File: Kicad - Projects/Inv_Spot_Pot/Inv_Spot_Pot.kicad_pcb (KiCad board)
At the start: 2 copper layers, 190 x 179.5 mm, 111 parts, among them J2 PWM, J3 Display_Power, J4 24V, J5 24V, J6 PWM, K1 Y14x-1C-xxDS, Q1 60N60, Q2 60N60, Q3 60N60, Q4 60N60, T1 Transformer_1P_2S, U2 LTV-817S

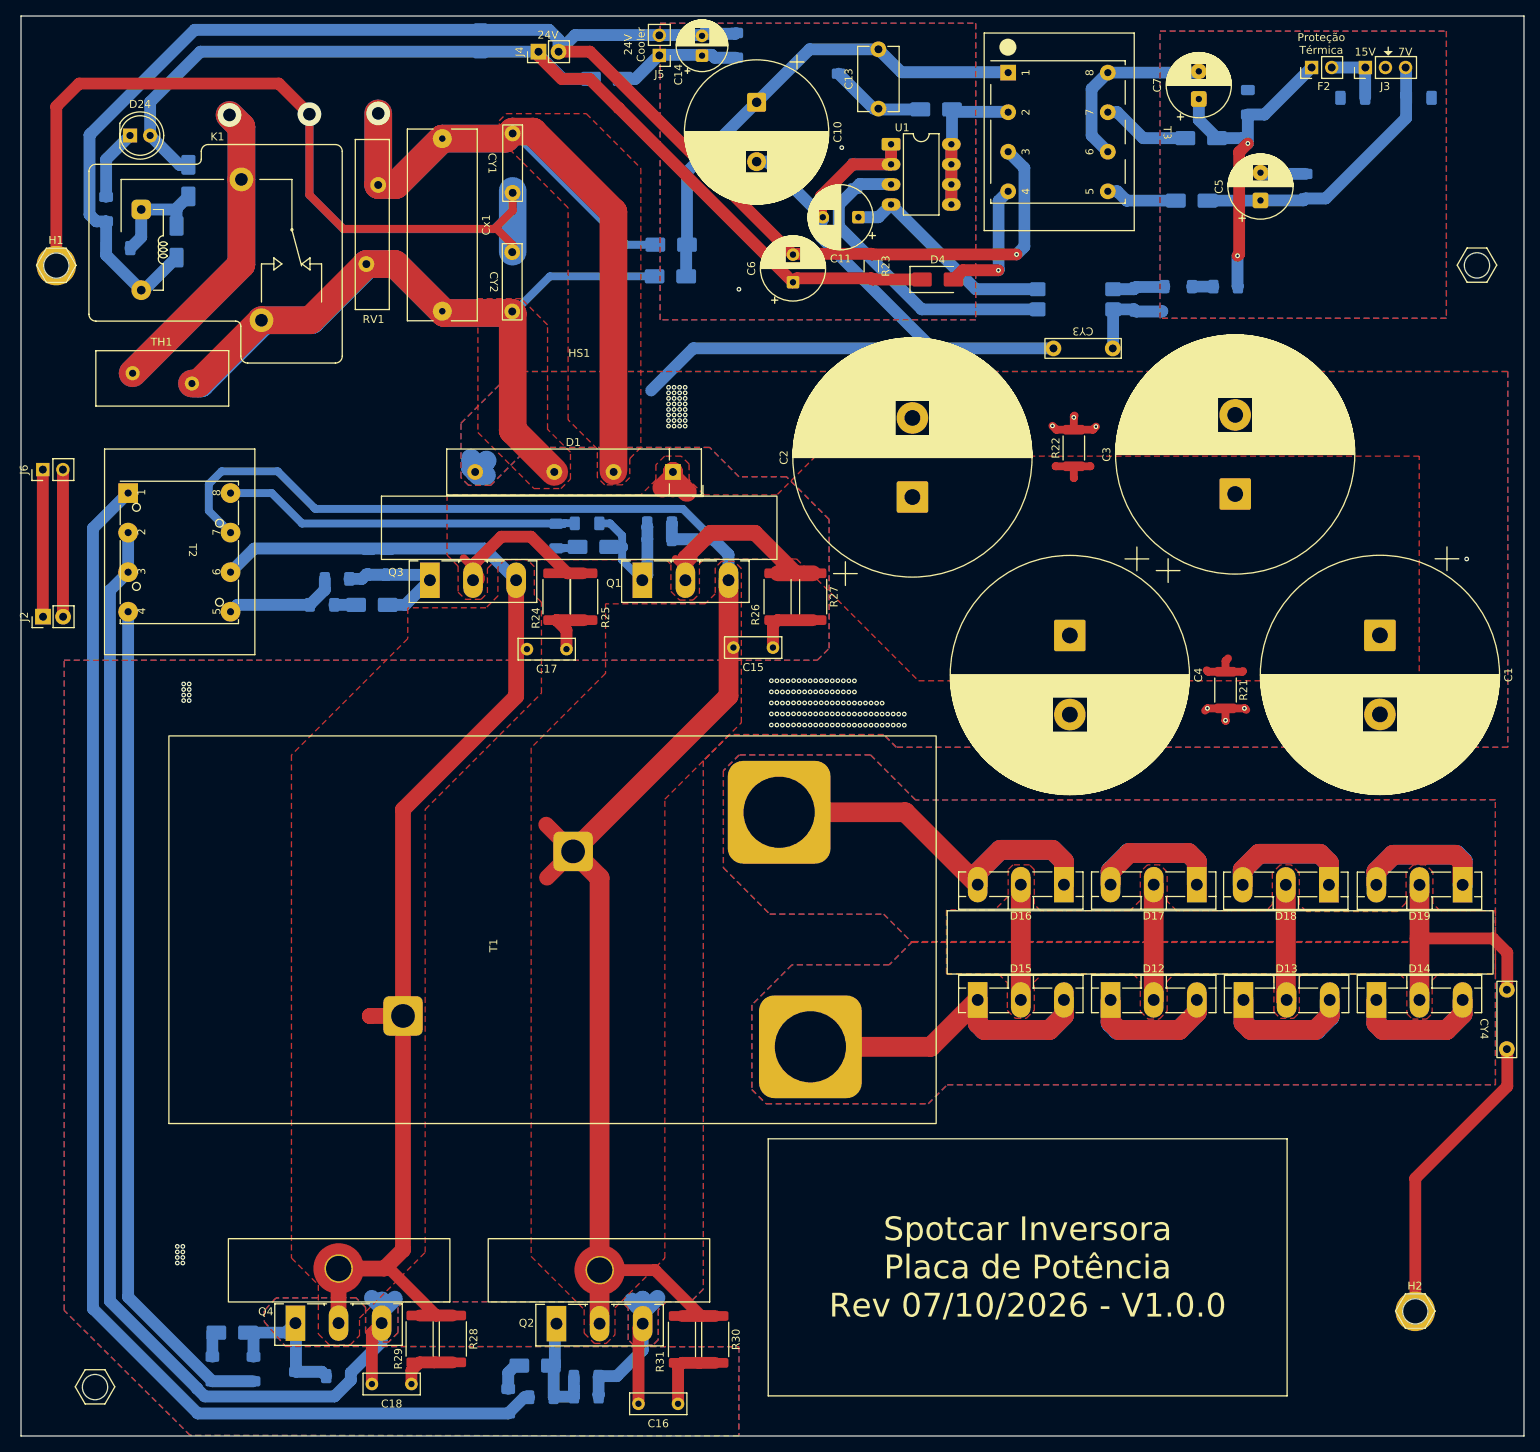
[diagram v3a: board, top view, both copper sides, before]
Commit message: Atualização de Footprints
Atualização de footprints dos transformadores principal e da fonte auxiliar
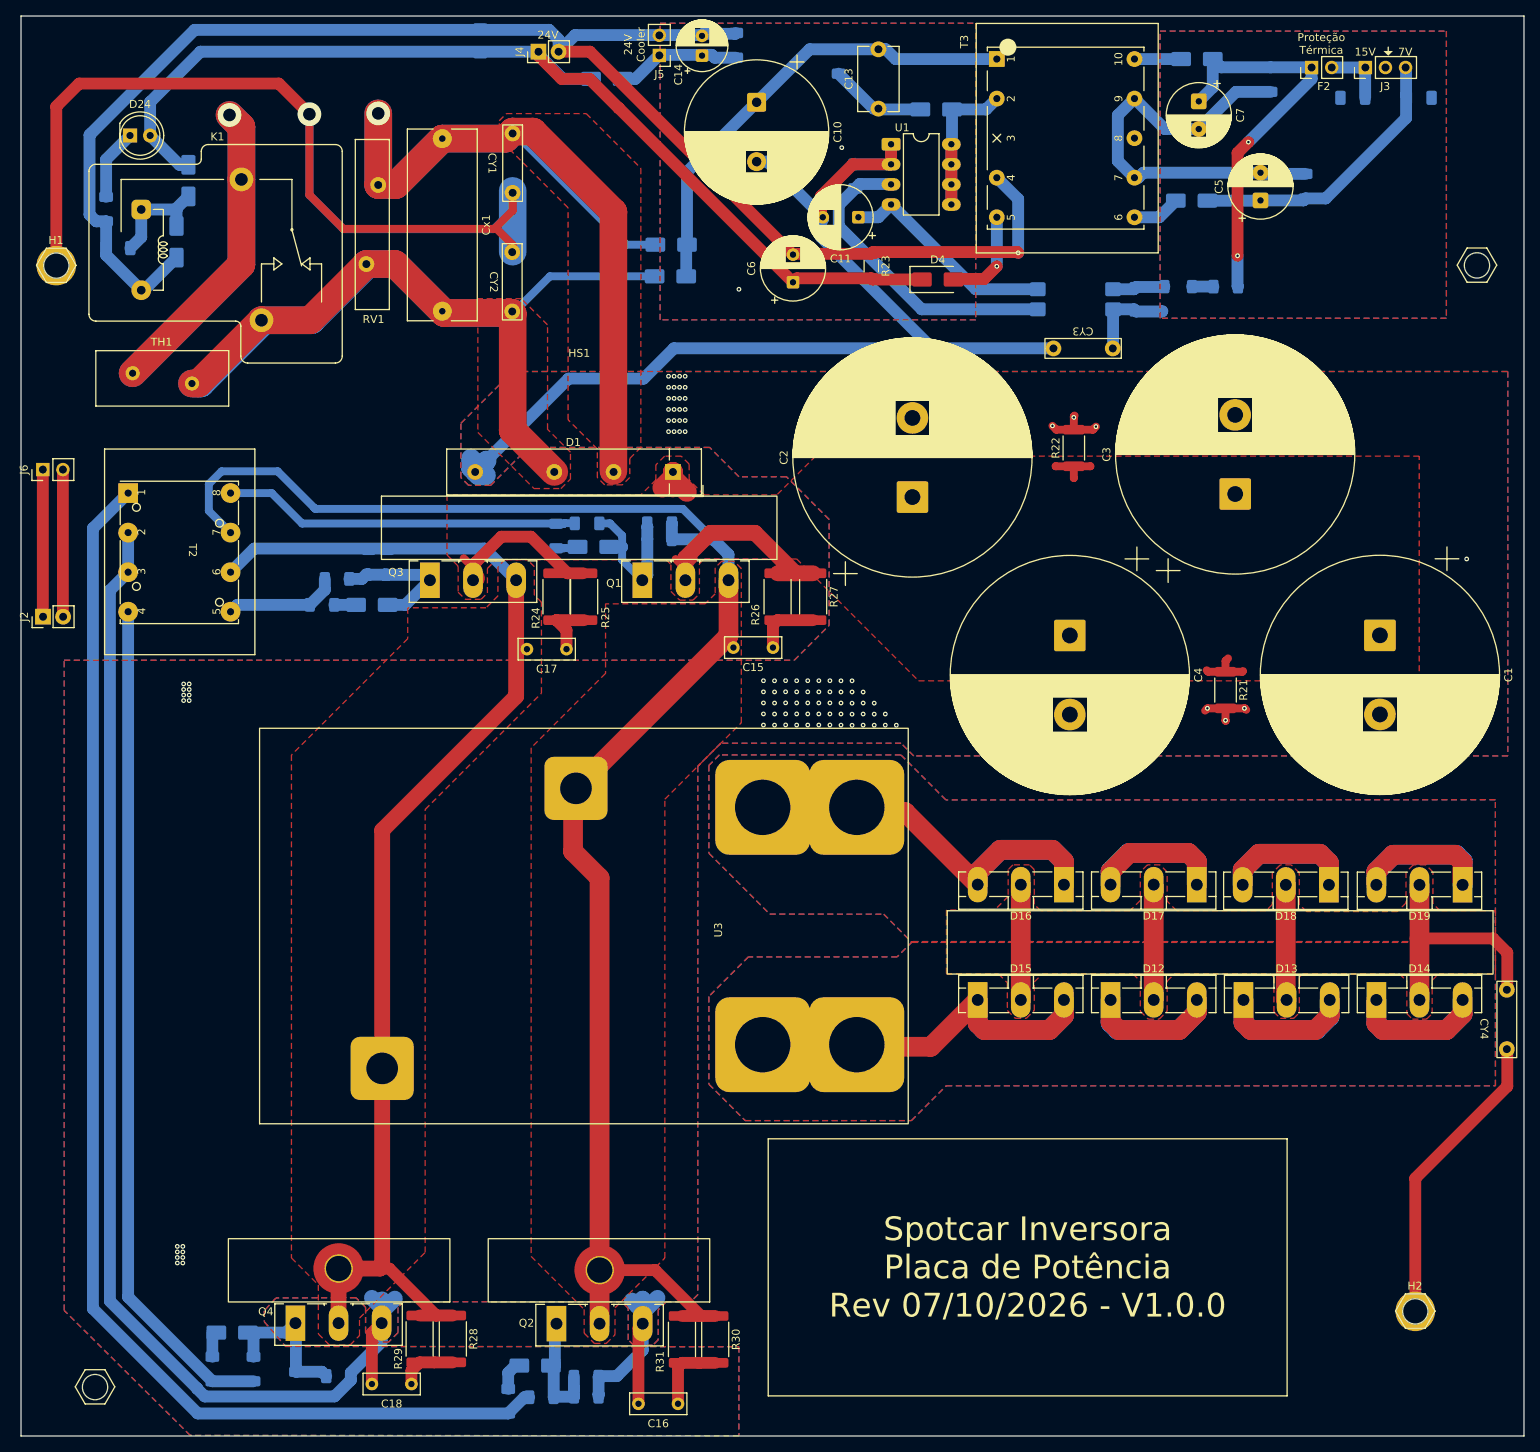
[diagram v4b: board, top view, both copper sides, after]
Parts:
- removed T1: Transformer_1P_2S, Custom_Transformer:Transformer_Toroid_THT_7032
- added U3: ~, Custom_Transformer:Sample-50x69.5-Double_Secondary, F.Cu at (103.3, 128.5)
- T3: footprint Custom_Transformer:EE25V-8T -> Transformer_THT:Transformer_Breve_TEZ-28x33
- moved T3 24.0 mm to (136.9, 18.4)
- moved D5 10.0 mm to (163.3, 18.4)
- moved R15 4.06 mm to (172.6, 21.0), turned to -90 degrees
- moved C7 0.29 mm to (163.5, 23.7), turned to -90 degrees
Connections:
- T3 pad 4: Net-(D4-A) -> GND_{24}
- T3 pad 5: Net-(D6-A) -> Net-(D4-A)
- T3 pad 6: GND -> Net-(D6-A)
- T3 pad 7: Net-(D5-A) -> GND
- T3 pad 8: GND -> (no net)
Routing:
- net Earth: track 325.8 -> 352.3 mm, vias 160 -> 104
- net GND: track 40.4 -> 65.8 mm
- net T-: track 226.9 -> 217.4 mm
- net Net-(D5-K): track 42.9 -> 50.6 mm
- net Net-(D5-A): track 11.2 -> 5.90 mm
- net T+: track 168.8 -> 164.3 mm
- net Net-(D4-A): track 16.6 -> 12.4 mm
- net GND_{24}: track 202.5 -> 199.2 mm
- net Net-(D6-A): track 9.09 -> 6.10 mm
- net 310_{Aux}: track 61.5 -> 59.3 mm
- net Net-(D3-A): track 26.9 -> 25.9 mm

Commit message: Removidos Resistores de 10k
Removidos os resistores de 10k

Melhorado alinhamento dos diodos de retificação

Próxima alteração coloca todos os SMDs no TOP
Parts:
- removed R13, R16, R3, R4: 10k, Resistor_SMD:R_1206_3216Metric_Pad1.30x1.75mm_HandSolder
- moved C20 2.09 mm to (95.4, 79.2)
- moved C22 2.00 mm to (58.9, 82.0)
- moved D18 0.10 mm to (180.1, 122.8)
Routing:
- net Out2: track 201.1 -> 197.5 mm
- net Earth: track 352.3 -> 349.8 mm
- net T-: track 217.4 -> 215.4 mm
- net Gate: track 18.9 -> 17.3 mm
- net ~{Gate}: track 14.5 -> 13.6 mm

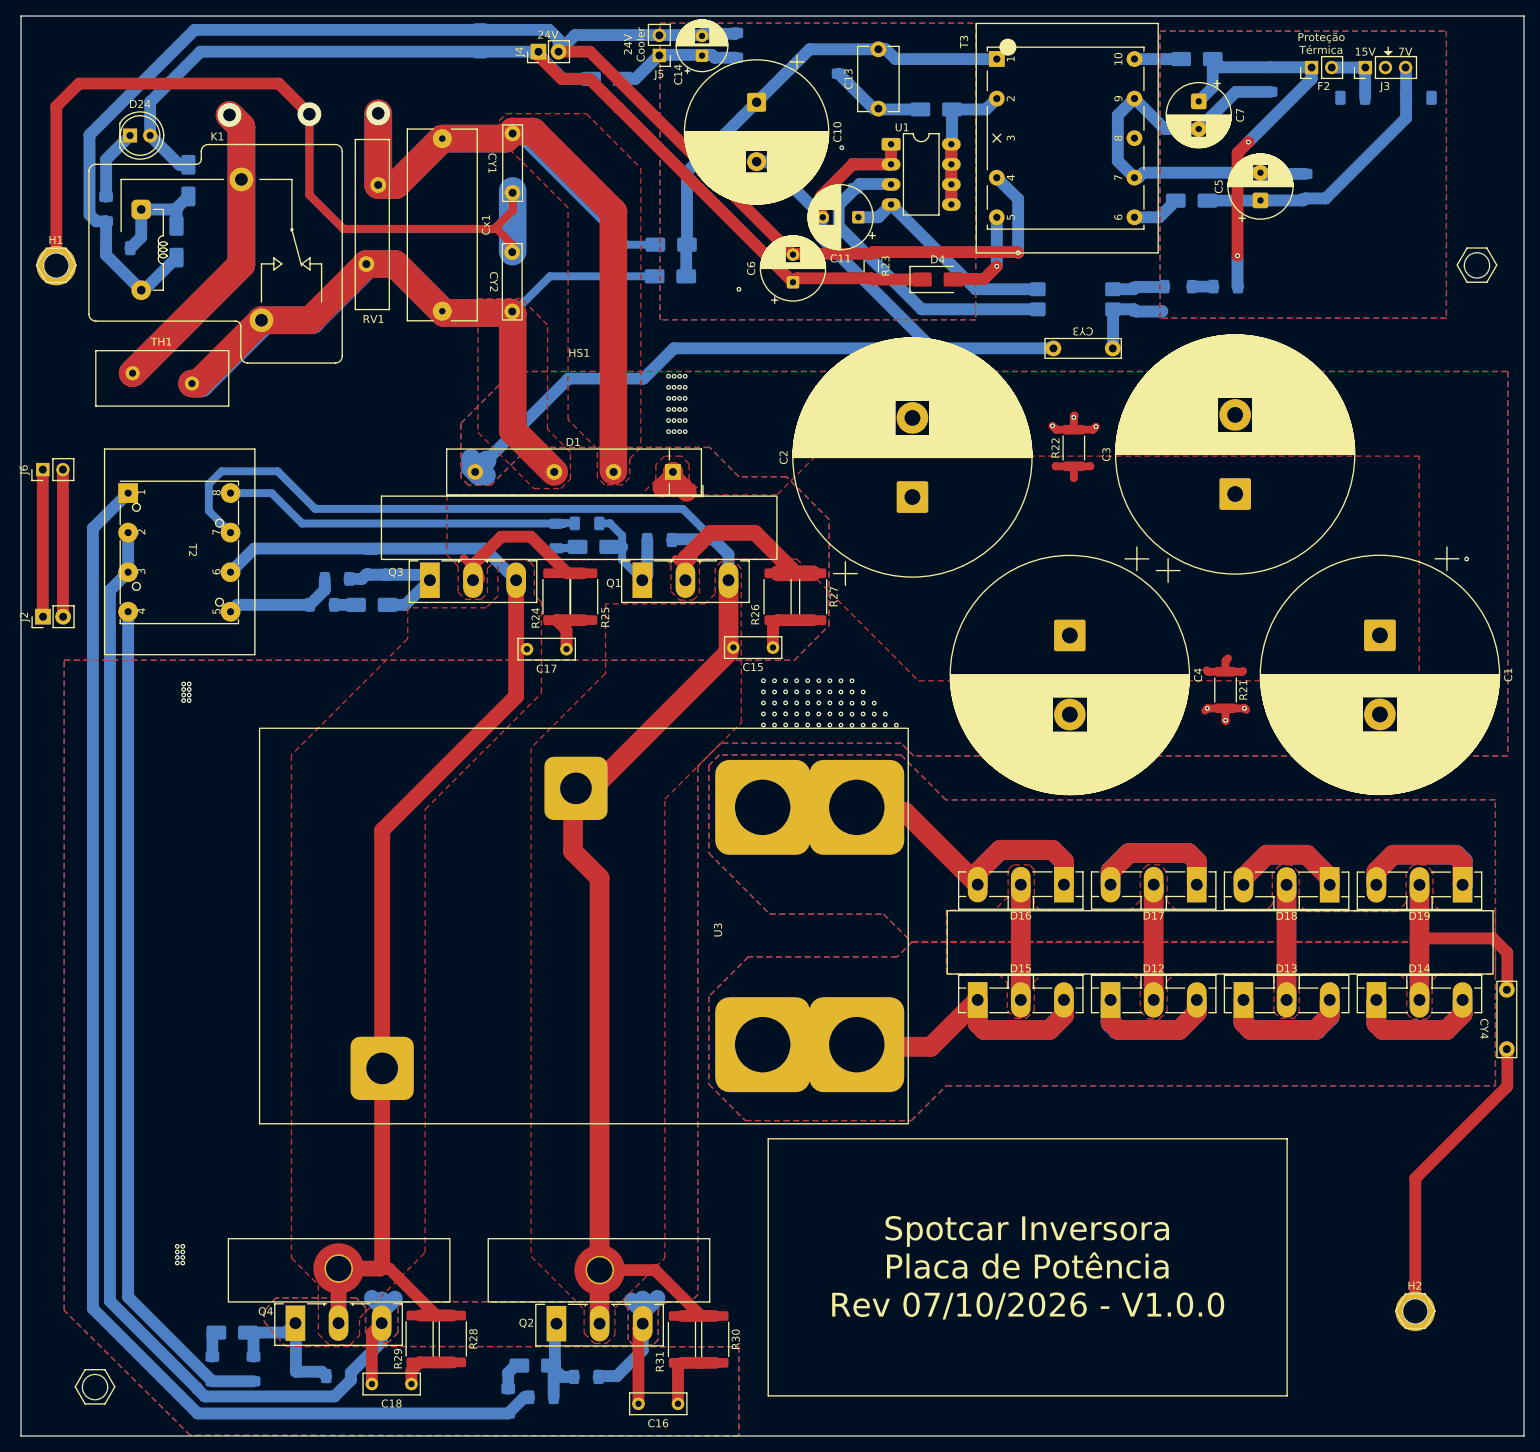
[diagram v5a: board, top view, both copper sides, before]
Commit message: SMD no TOP
Todos SMDs transferidos para camada TOP
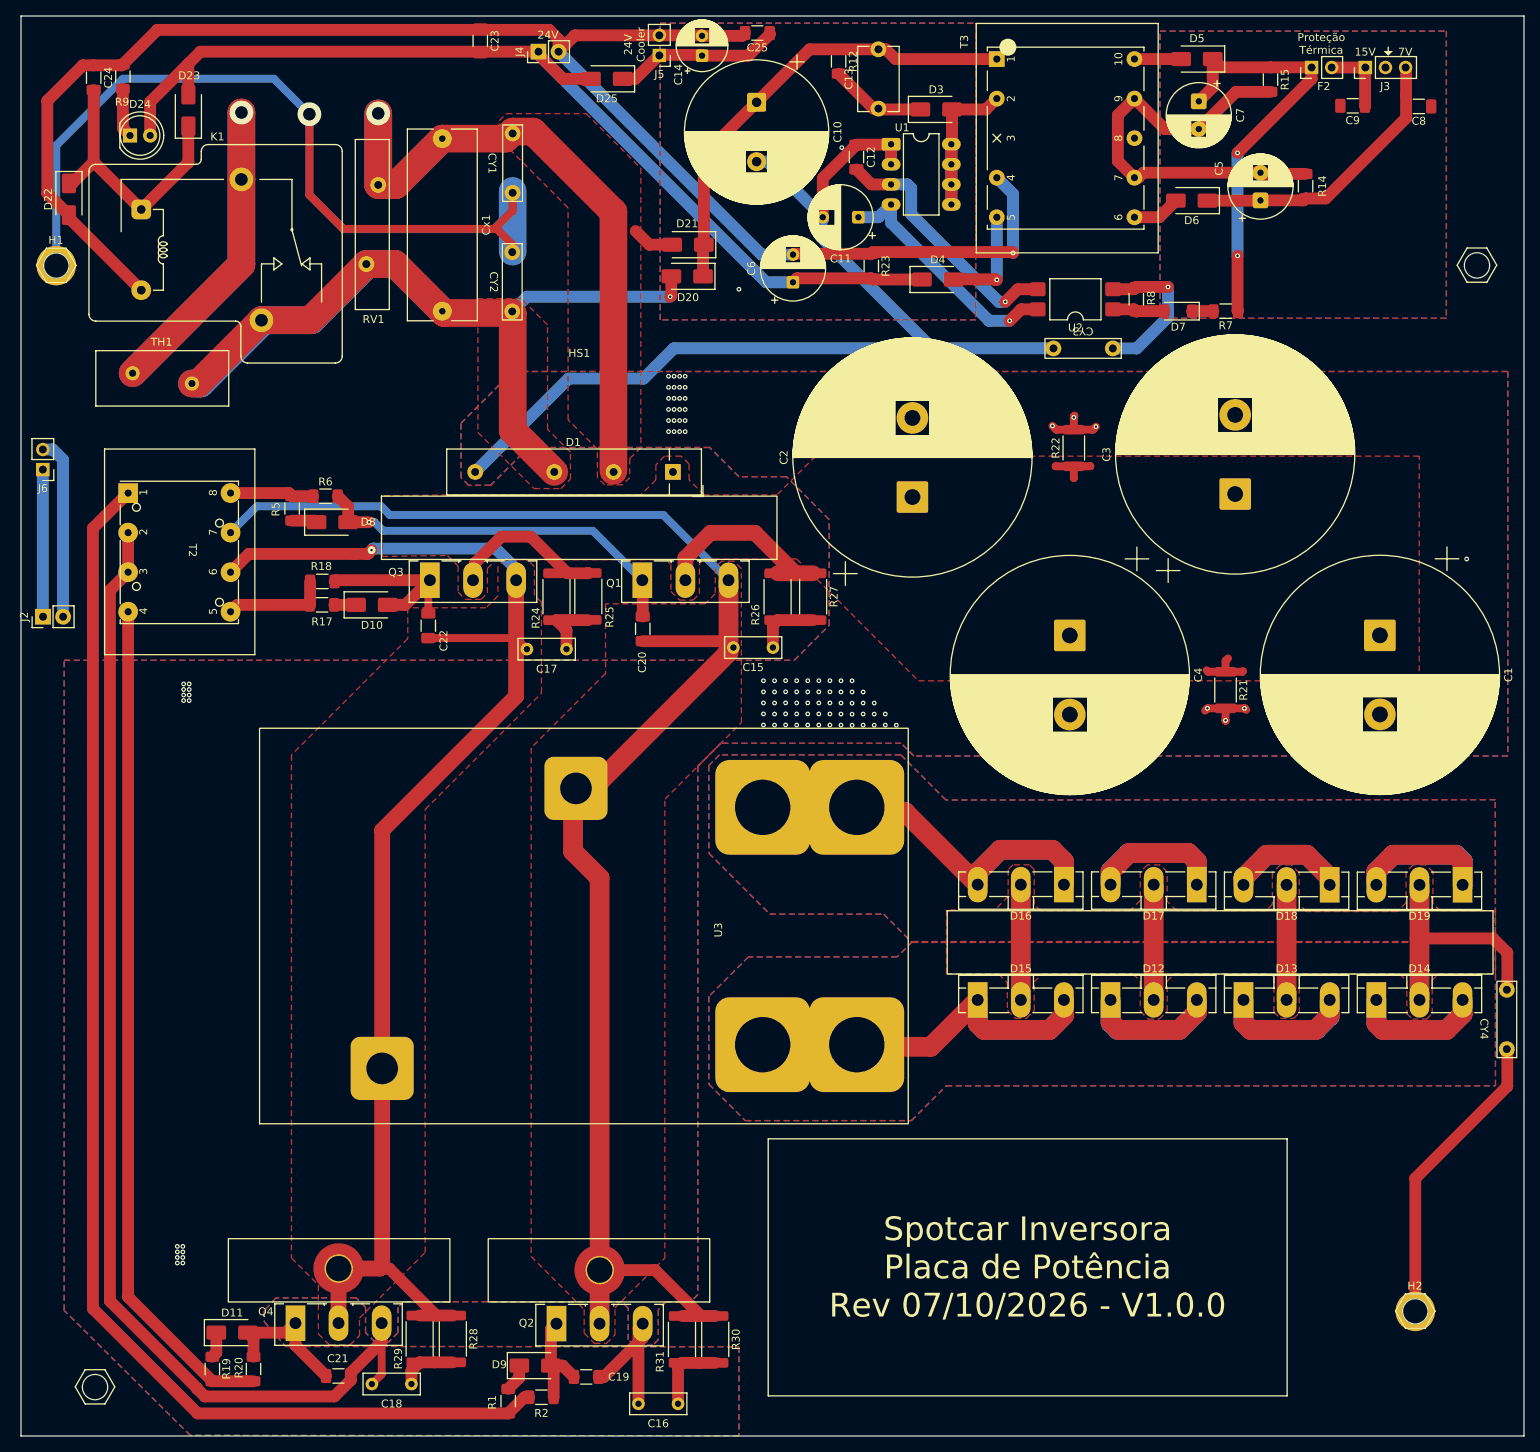
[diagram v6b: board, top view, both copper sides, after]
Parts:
- C12, C19, C20, C21, C22, C23, C24, C25, C8, C9, D10, D11, D20, D21, D22, D23, D25, D3, D5, D6, D7, D8, D9, R1, R12, R14, R15, R17, R18, R19, R2, R20, R5, R6, R7, R8, R9, U2: moved to F.Cu
- moved R5 33.6 mm to (48.9, 75.2)
- moved R6 33.2 mm to (53.1, 73.7)
- moved D8 33.1 mm to (54.0, 77.0)
- moved C24 21.8 mm to (23.8, 20.8), turned to -90 degrees
- moved R9 16.9 mm to (27.5, 20.6), turned to 90 degrees
- moved D22 14.6 mm to (20.7, 36.1)
- moved C20 11.4 mm to (93.2, 90.4), turned to -90 degrees
- moved C22 10.8 mm to (66.1, 90.0), turned to -90 degrees
- moved D23 8.87 mm to (35.8, 24.9)
- moved C25 3.12 mm to (107.7, 15.1), turned to 180 degrees
- moved D7 3.10 mm to (160.9, 50.3)
- moved R7 3.10 mm to (166.9, 50.3)
- moved C12 2.41 mm to (120.2, 30.8)
- moved D20 2.13 mm to (99.0, 41.9)
- moved D21 2.13 mm to (98.9, 45.9)
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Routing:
- net PWM: track 45.2 -> 10.6 mm
- net Gate: track 17.3 -> 48.7 mm, vias 0 -> 1
- net Earth: track 349.8 -> 319.7 mm
- net /Soft_Start-24V/AC_{2}: track 131.3 -> 103.4 mm
- net Net-(D22-K): track 14.2 -> 34.8 mm
- net 310V: track 74.5 -> 59.1 mm
- net T+: track 164.3 -> 178.1 mm, vias 0 -> 1
- net T-: track 215.4 -> 202.9 mm
- net GND: track 65.8 -> 73.9 mm, vias 0 -> 1
- net Net-(U1-FB): track 39.9 -> 32.4 mm, vias 0 -> 1
- net Gate1: track 17.4 -> 23.0 mm
- net /Soft_Start-24V/~{AC{1}}: track 141.1 -> 135.6 mm, vias 0 -> 1
- net 24V-Cooler: track 15.8 -> 21.2 mm
- net /PWM_L: track 18.6 -> 22.9 mm
- net Net-(U1-Vcc): track 27.8 -> 31.4 mm, vias 0 -> 1
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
